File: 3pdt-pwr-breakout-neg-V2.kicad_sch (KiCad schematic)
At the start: 42 parts, among them Q1 DMP3099L, SW1 SW_3PDT, U1 TLV76701DRVR, U2 LM2664M6X/NOPB, U3 LM2664M6X/NOPB

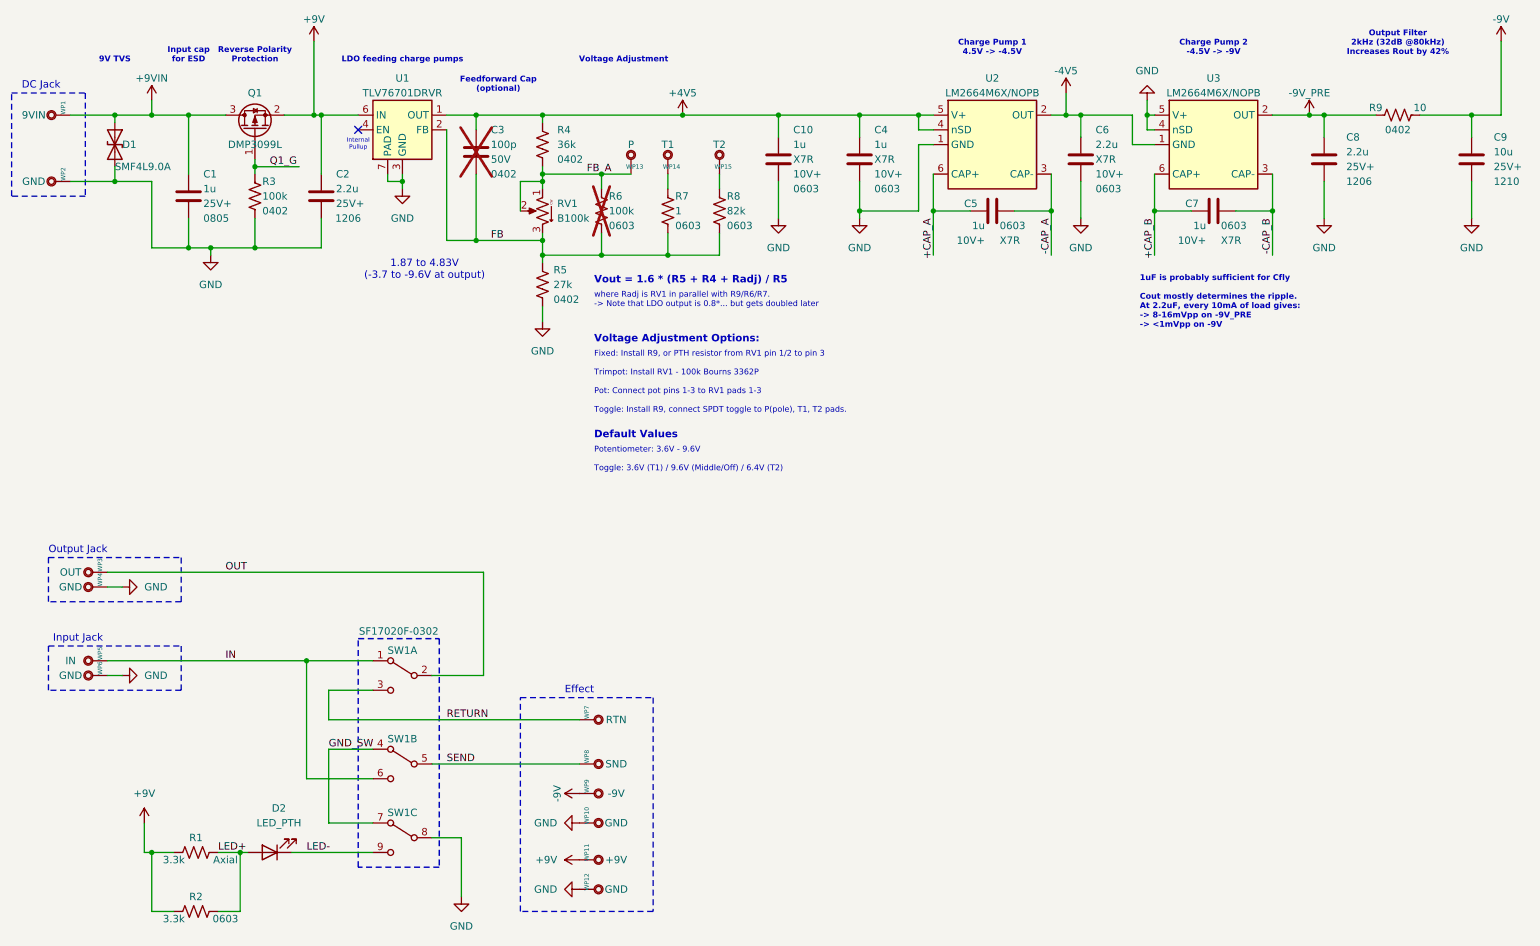
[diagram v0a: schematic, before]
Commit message: Updated R amd C symbols
Changed field sizes/visibilities. Should pull into PCB too before review
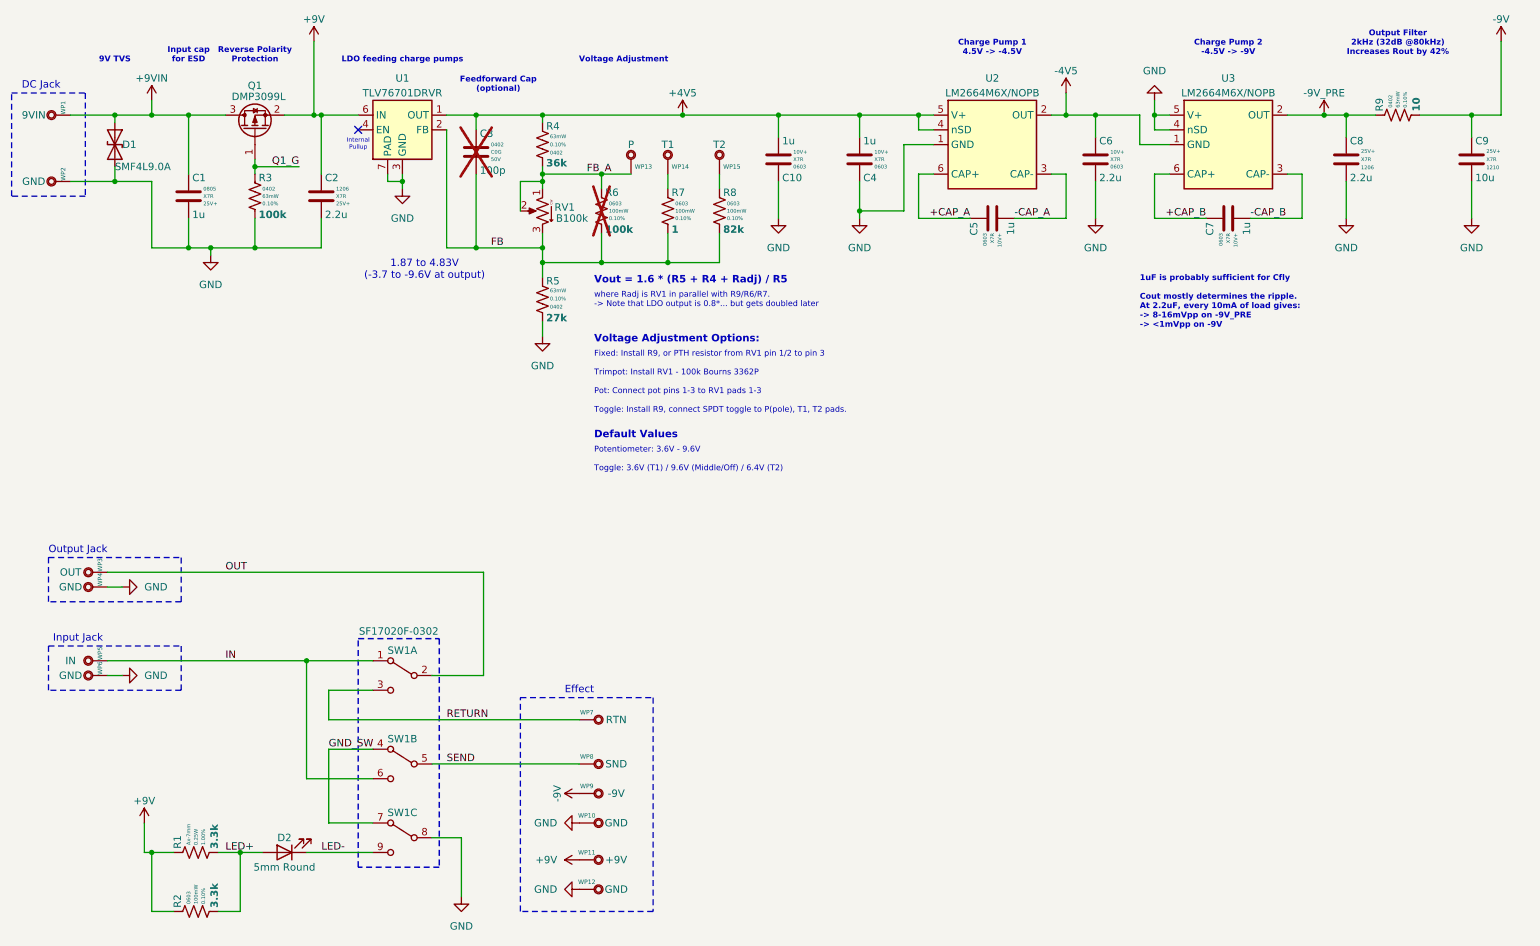
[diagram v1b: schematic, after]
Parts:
- C1: footprint Capacitor_SMD:C_0805:2012Metric -> Capacitor_SMD:C_0805_2012Metric; Case/Package 0805 -> (none); Package/Case (none) -> 0805
- C10, C4, C5, C7: value 2.2u -> 1u; Case/Package 0603 -> (none); Package/Case (none) -> 0603
- C2, C8: Case/Package 1206 -> (none); Package/Case (none) -> 1206
- C3: Case/Package 0402 -> (none); Package/Case (none) -> 0402
- C6: Case/Package 0603 -> (none); Package/Case (none) -> 0603
- C9: Case/Package 1210 -> (none); Package/Case (none) -> 1210
- D2: symbol #gplm:dio/DIO-1006-0001 -> #gplm:led/LED-2000-0000; IPN DIO-1006-0001 -> LED-2000-0000; Package/Case (none) -> 5mm Round
- R1: Case/Package Axial -> (none); Composition (none) -> Metal Film; Height (none) -> 2.6mm; Package/Case (none) -> Ax-7mm; Temp Coefficient (none) -> 100ppm; Voltage (none) -> 250V
- R2, R6, R7, R8: Case/Package 0603 -> (none); Composition (none) -> Thin Film; Height (none) -> 0.55mm; Package/Case (none) -> 0603; Temp Coefficient (none) -> 25ppm; Voltage (none) -> 75V
- R3, R4, R5, R9: Case/Package 0402 -> (none); Composition (none) -> Thin Film; Height (none) -> 0.35mm; Package/Case (none) -> 0402; Temp Coefficient (none) -> 25ppm; Voltage (none) -> 50V
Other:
- moved on the sheet: C10, C4, C5, C6, C7, C8, D2, R5, U3

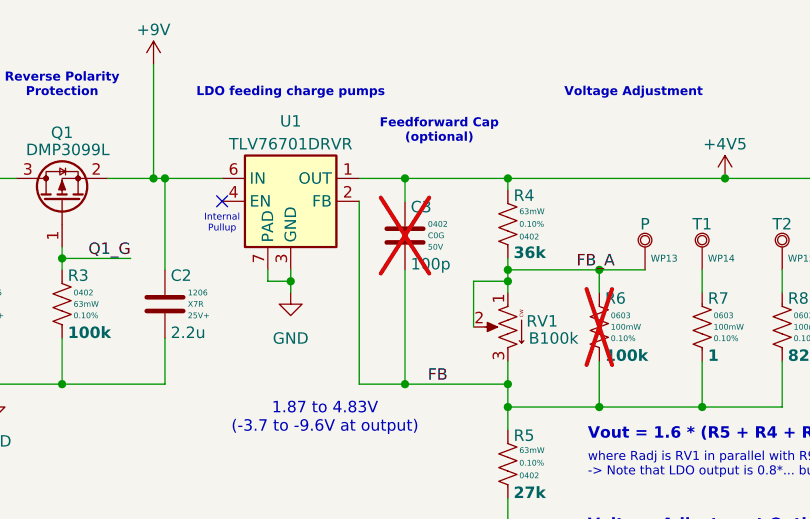
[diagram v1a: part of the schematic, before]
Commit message: Moved wire pads, clearing warnings. Good to fab?
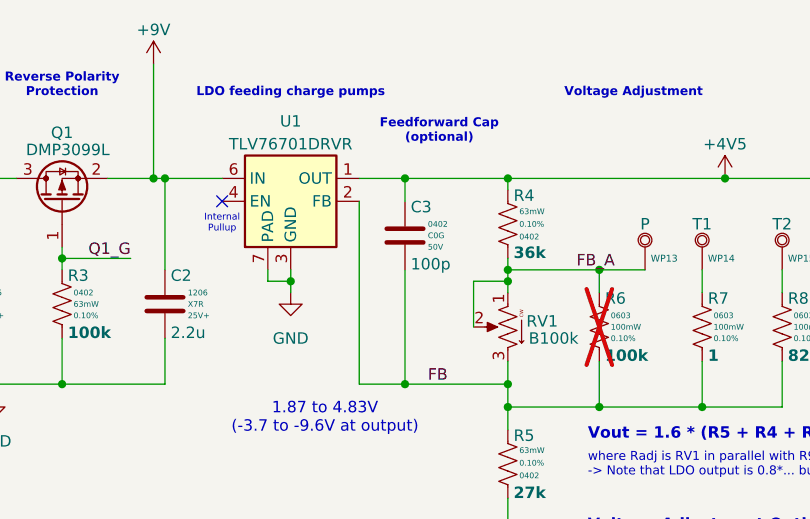
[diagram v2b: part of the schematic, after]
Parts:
- C3: symbol #gplm:cap/CAP-4001-0101 -> #gplm:cap/CAP-4001-0100; Capacitance 100p -> 10p; IPN CAP-4001-0101 -> CAP-4001-0100; MPN GRM1555C1H101GA01D -> GRM1555C1H100GA01D; now fitted
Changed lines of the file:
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@@
 	)
 	(symbol
-		(lib_id "#gplm:cap/CAP-4001-0101")
+		(lib_id "#gplm:cap/CAP-4001-0100")
 		(at 99.06 44.45 0)
 		(unit 1)
@@
 		(in_bom yes)
 		(on_board yes)
-		(dnp yes)
+		(dnp no)
 		(property "Reference" "C3"
 			(at 99.695 41.275 0)
@@
 			)
 		)
-		(property "Datasheet" "https://www.murata.com/en-us/products/productdetail?partno=GRM1555C1H101GA01D%23"
+		(property "Datasheet" "https://www.murata.com/en-us/products/productdetail?partno=GRM1555C1H100GA01D%23"
 			(at 99.06 44.45 0)
 			(effects
@@
 			)
 		)
-		(property "Description" "CAP SMD 100p 0402 50V C0G +/-2%"
+		(property "Description" "CAP SMD 10p 0402 50V C0G +/-2%"
 			(at 99.06 44.45 0)
 			(effects
@@
 			)
 		)
-		(property "IPN" "CAP-4001-0101"
+		(property "IPN" "CAP-4001-0100"
 			(at 99.06 44.45 0)
 			(effects
@@
 			)
 		)
-		(property "MPN" "GRM1555C1H101GA01D"
+		(property "MPN" "GRM1555C1H100GA01D"
 			(at 99.06 44.45 0)
 			(effects
@@
 			)
 		)
-		(property "Capacitance" "100p"
+		(property "Capacitance" "10p"
 			(at 99.06 44.45 0)
 			(effects

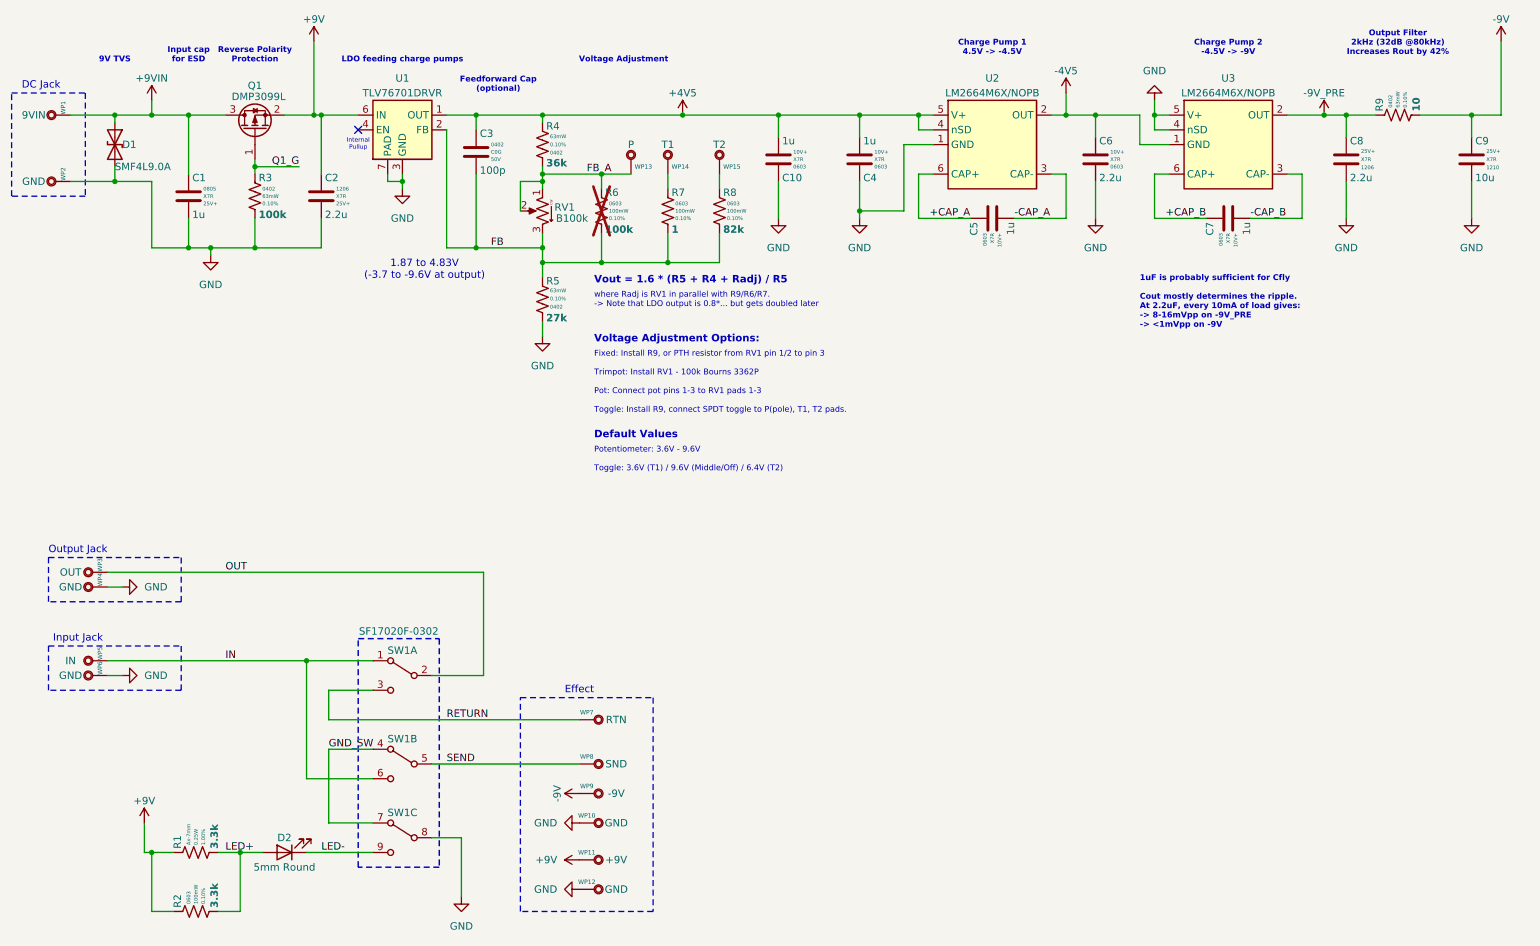
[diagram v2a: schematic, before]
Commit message: Changed LDO and added negative LDO
Changed LDO to a leaded package and added an optional negative LDO. Layout changes implemented, going to review and order.
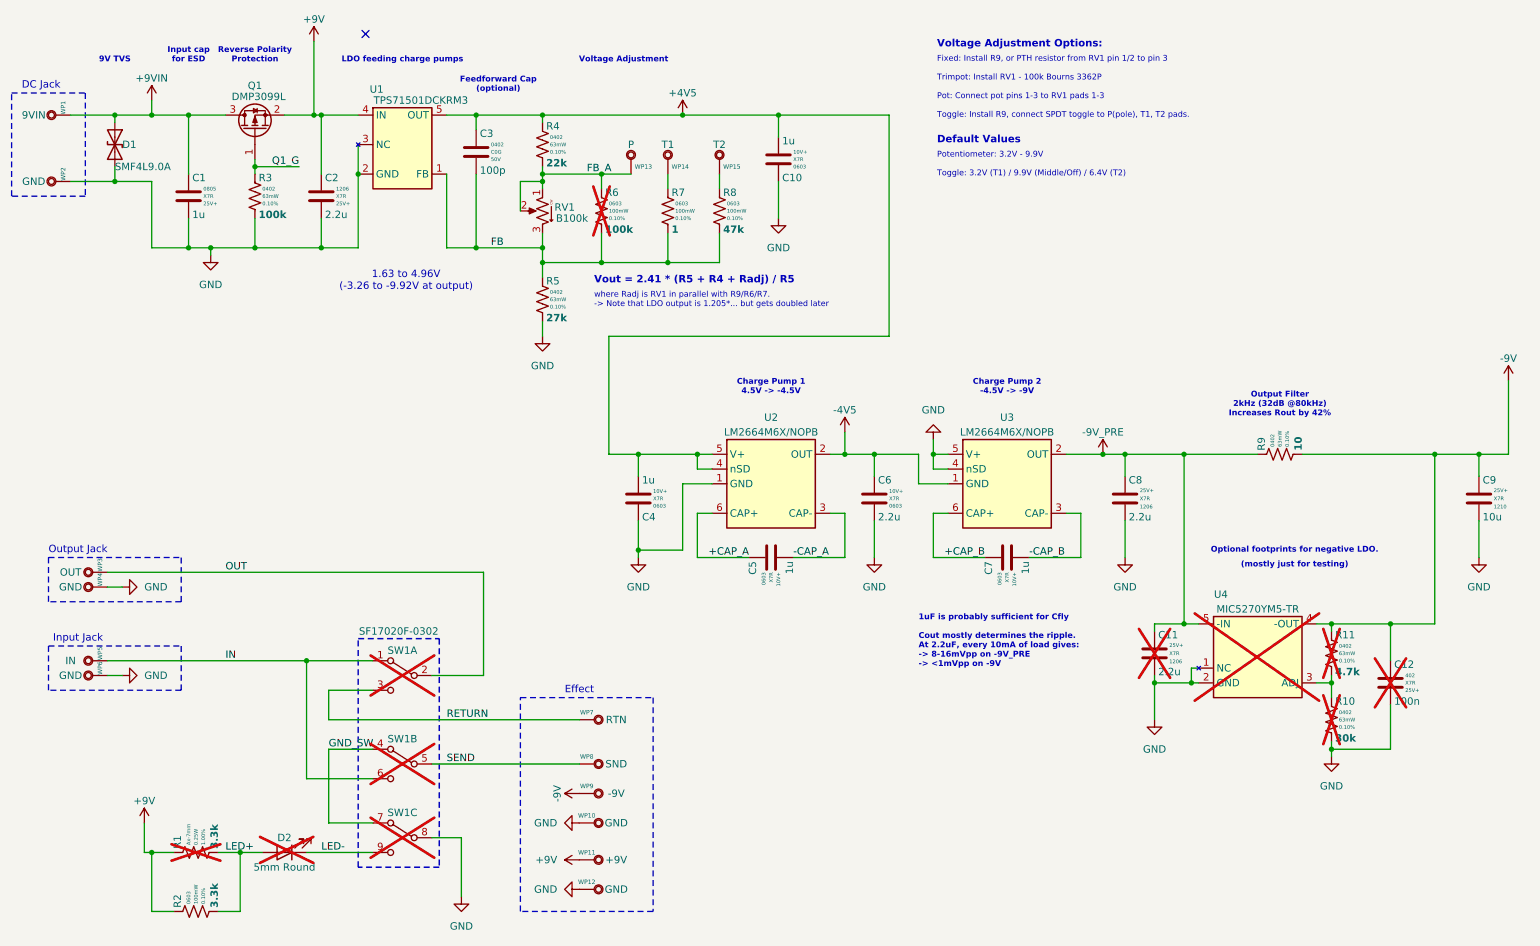
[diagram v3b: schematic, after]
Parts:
- removed U1: TLV76701DRVR, Package_SON:WSON-6-1EP_2x2mm_P0.65mm_EP1x1.6mm, symbol #gplm:reg/REG-1005-0001
- added C11: 2.2u, Capacitor_SMD:C_1206_3216Metric, symbol #gplm:cap/CAP-4106-02U2
- added C12: 100n, Capacitor_SMD:C_0402_1005Metric, symbol #gplm:cap/CAP-4103-100N
- added R10: 30k, Resistor_SMD:R_0402_1005Metric, symbol #gplm:res/RES-2002-030K
- added R11: 4.7k, Resistor_SMD:R_0402_1005Metric, symbol #gplm:res/RES-2002-04K7
- added U1: TPS71501DCKRM3, Package_TO_SOT_SMD:SOT-353_SC-70-5, symbol #gplm:reg/REG-1007-0001
- added U4: MIC5270YM5-TR, Package_TO_SOT_SMD:SOT-23-5, symbol #gplm:reg/REG-1008-0001
- D2, R1, SW1: now not fitted; now left out of the parts list
- R4: value 36k -> 22k; symbol #gplm:res/RES-2002-036K -> #gplm:res/RES-2002-022K; IPN RES-2002-036K -> RES-2002-022K; MPN RT0402BRD0736KL -> RT0402BRD0722KL; Resistance 36k -> 22k
- R6: now left out of the parts list
- R8: value 82k -> 47k; symbol #gplm:res/RES-2001-082K -> #gplm:res/RES-2001-047K; IPN RES-2001-082K -> RES-2001-047K; MPN RT0603BRD0782KL -> RT0603BRD0747KL; Resistance 82k -> 47k
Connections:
- net +4V5: now also U1.5 (OUT)
- net +9V: now also U1.4 (IN)
- net -9V: now also C12.1, R11.1, U4.4 (-OUT)
- net -9V_PRE: now also C11.1, U4.5 (-IN)
- net FB: now also U1.1 (FB)
- net GND: now also C11.2, C12.2, R10.2, U1.2 (GND), U1.3 (NC), U4.1 (NC), U4.2 (GND)
- new net: R10.1, R11.2, U4.3 (ADJ)
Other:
- note added: "(mostly just for testing)"
- note added: "1.63 to 4.96V (-3.26 to -9.92V at output)"
- note added: "Optional footprints for negative LDO."
- note added: "Potentiometer: 3.2V - 9.9V Toggle: 3.2V (T1) / 9.9V (Middle/Off) / 6.4V (T2)"
- note added: "Vout = 2.41 * (R5 + R4 + Radj) / R5"
- note added: "where Radj is RV1 in parallel with R9/R6/R7. -> Note that LDO output is 1.205*... but gets doubled later"
- note removed: "1.87 to 4.83V (-3.7 to -9.6V at output)"
- note removed: "Internal Pullup"
- note removed: "Potentiometer: 3.6V - 9.6V Toggle: 3.6V (T1) / 9.6V (Middle/Off) / 6.4V (T2)"
- note removed: "Vout = 1.6 * (R5 + R4 + Radj) / R5"
- note removed: "where Radj is RV1 in parallel with R9/R6/R7. -> Note that LDO output is 0.8*... but gets doubled later"
- moved on the sheet: C4, C5, C6, C7, C8, C9, R9, U2, U3

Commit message: Generated fab files
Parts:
- RV1: now not fitted
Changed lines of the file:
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@@
 		(in_bom yes)
 		(on_board yes)
-		(dnp no)
+		(dnp yes)
 		(property "Reference" "RV1"
 			(at 114.3 53.975 0)
